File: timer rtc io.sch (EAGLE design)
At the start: 78 parts, among them T1 BC547, U1 74HC245, U10 74HC688, U11 74LS30N, U12 74LS00N, U13 74HC32, U14 74HC04, U15 74HC08, U16 74HC688, U17 74HC138, U18 74HC138, U19 74HC573, U2 74HC245, U20 74HC573, U21 74HC573, U22 74HC573, U23 74HC573, U24 NE555, U3 74HC245, U4 74HC688, U6 74HC74, U7 74HC590, U8 74HC688, U9 BQ4845, X1 32.768KHz, Y1 4.096MHz

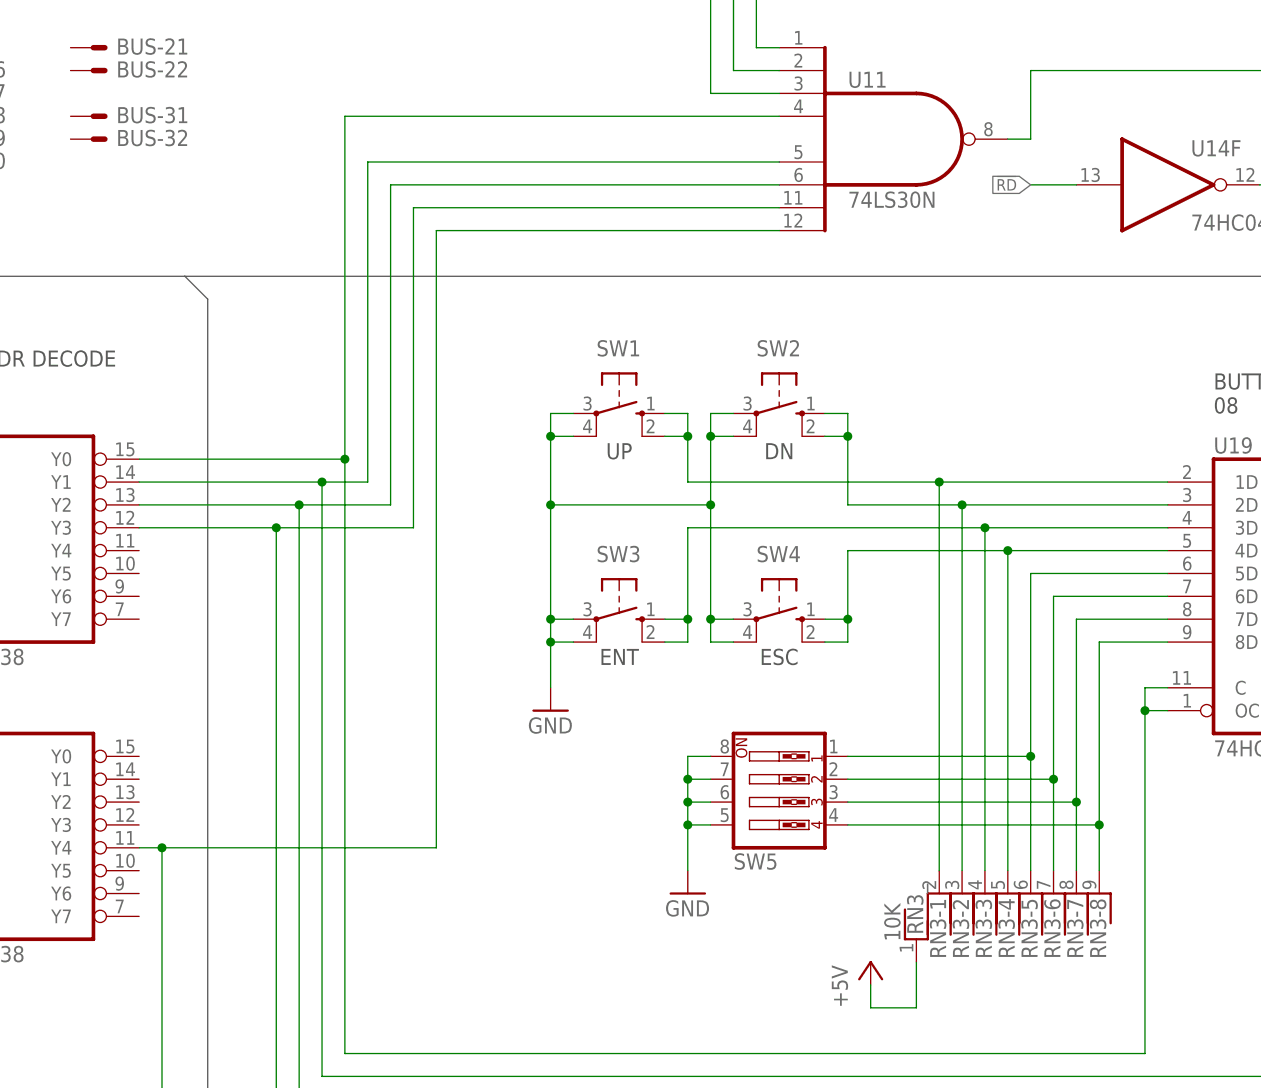
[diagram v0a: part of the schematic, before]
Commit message: Annotate SW5 DIP switch positions
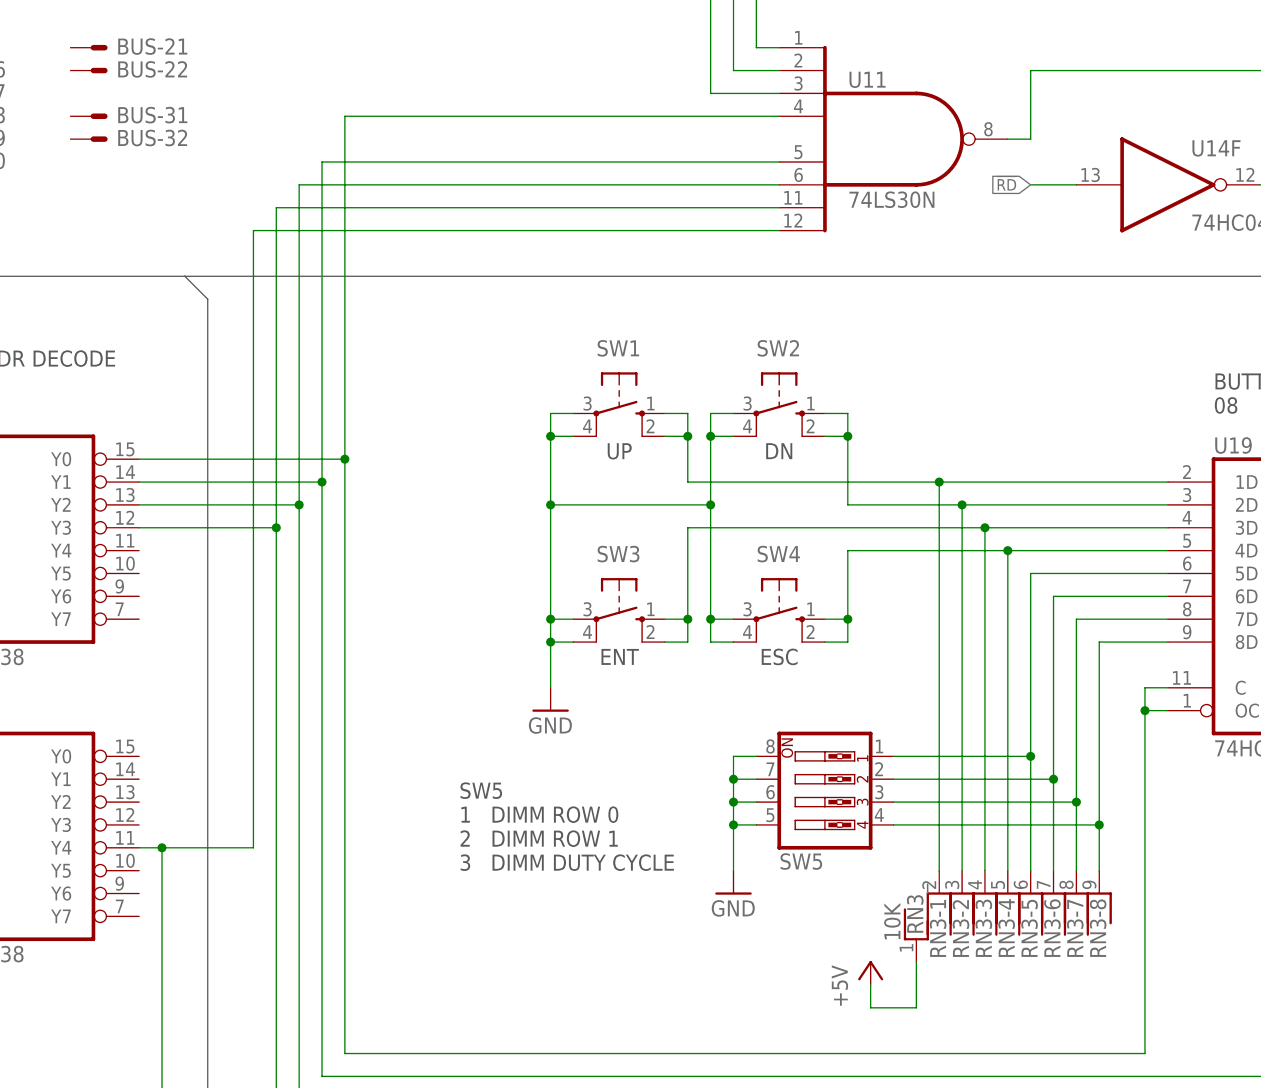
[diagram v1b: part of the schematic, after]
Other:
- note added: "SW5 1 DIMM ROW 0 2 DIMM ROW 1 3 DIMM DUTY CYCLE"
- note added: "TODO"
- moved on the sheet: SW5
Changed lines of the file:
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@@
 <?xml version="1.0" encoding="utf-8"?>
 <!DOCTYPE eagle SYSTEM "eagle.dtd">
-<eagle version="9.5.2">
+<eagle version="9.6.1">
 <drawing>
 <settings>
@@
 <text x="228.6" y="-139.7" size="1.778" layer="97">R4=560R R5=560R ~66% D/C ~8.6KHZ
 R4=1K5 R5=150R ~91% D/C ~8KHZ</text>
+<text x="208.28" y="-38.1" size="1.778" layer="97">SW5
+1   DIMM ROW 0
+2   DIMM ROW 1
+3   DIMM DUTY CYCLE</text>
+<text x="302.26" y="-137.16" size="3.81" layer="90">TODO</text>
 </plain>
 <instances>
@@
 <attribute name="VALUE" x="93.98" y="124.46" size="1.778" layer="96"/>
 </instance>
-<instance part="SW5" gate="A" x="243.84" y="-30.48" smashed="yes" rot="MR180">
-<attribute name="NAME" x="238.76" y="-36.195" size="1.778" layer="95" rot="MR180"/>
-<attribute name="VALUE" x="238.76" y="-20.32" size="1.778" layer="96" rot="MR180"/>
+<instance part="SW5" gate="A" x="248.92" y="-30.48" smashed="yes" rot="MR180">
+<attribute name="NAME" x="243.84" y="-36.195" size="1.778" layer="95" rot="MR180"/>
+<attribute name="VALUE" x="243.84" y="-20.32" size="1.778" layer="96" rot="MR180"/>
 </instance>
-<instance part="GND20" gate="1" x="233.68" y="-40.64" smashed="yes">
-<attribute name="VALUE" x="231.14" y="-43.18" size="1.778" layer="96"/>
+<instance part="GND20" gate="1" x="238.76" y="-40.64" smashed="yes">
+<attribute name="VALUE" x="236.22" y="-43.18" size="1.778" layer="96"/>
 </instance>
 <instance part="U16" gate="A" x="109.22" y="-17.78" smashed="yes">
@@
 <pinref part="SW5" gate="A" pin="8"/>
 <pinref part="GND20" gate="1" pin="GND"/>
-<wire x1="236.22" y1="-25.4" x2="233.68" y2="-25.4" width="0.1524" layer="91"/>
-<wire x1="233.68" y1="-25.4" x2="233.68" y2="-27.94" width="0.1524" layer="91"/>
+<wire x1="241.3" y1="-25.4" x2="238.76" y2="-25.4" width="0.1524" layer="91"/>
+<wire x1="238.76" y1="-25.4" x2="238.76" y2="-27.94" width="0.1524" layer="91"/>
 <pinref part="SW5" gate="A" pin="7"/>
-<wire x1="233.68" y1="-27.94" x2="233.68" y2="-30.48" width="0.1524" layer="91"/>
-<wire x1="233.68" y1="-30.48" x2="233.68" y2="-33.02" width="0.1524" layer="91"/>
-<wire x1="233.68" y1="-33.02" x2="233.68" y2="-38.1" width="0.1524" layer="91"/>
-<wire x1="236.22" y1="-27.94" x2="233.68" y2="-27.94" width="0.1524" layer="91"/>
-<junction x="233.68" y="-27.94"/>
+<wire x1="238.76" y1="-27.94" x2="238.76" y2="-30.48" width="0.1524" layer="91"/>
+<wire x1="238.76" y1="-30.48" x2="238.76" y2="-33.02" width="0.1524" layer="91"/>
+<wire x1="238.76" y1="-33.02" x2="238.76" y2="-38.1" width="0.1524" layer="91"/>
+<wire x1="241.3" y1="-27.94" x2="238.76" y2="-27.94" width="0.1524" layer="91"/>
+<junction x="238.76" y="-27.94"/>
 <pinref part="SW5" gate="A" pin="6"/>
-<wire x1="236.22" y1="-30.48" x2="233.68" y2="-30.48" width="0.1524" layer="91"/>
-<junction x="233.68" y="-30.48"/>
+<wire x1="241.3" y1="-30.48" x2="238.76" y2="-30.48" width="0.1524" layer="91"/>
+<junction x="238.76" y="-30.48"/>
 <pinref part="SW5" gate="A" pin="5"/>
-<wire x1="236.22" y1="-33.02" x2="233.68" y2="-33.02" width="0.1524" layer="91"/>
-<junction x="233.68" y="-33.02"/>
+<wire x1="241.3" y1="-33.02" x2="238.76" y2="-33.02" width="0.1524" layer="91"/>
+<junction x="238.76" y="-33.02"/>
 </segment>
 <segment>
@@
 <pinref part="SW5" gate="A" pin="1"/>
 <wire x1="271.78" y1="-25.4" x2="271.78" y2="-38.1" width="0.1524" layer="91"/>
-<wire x1="251.46" y1="-25.4" x2="271.78" y2="-25.4" width="0.1524" layer="91"/>
+<wire x1="256.54" y1="-25.4" x2="271.78" y2="-25.4" width="0.1524" layer="91"/>
 <junction x="271.78" y="-25.4"/>
 </segment>
@@
 <pinref part="SW5" gate="A" pin="2"/>
 <wire x1="274.32" y1="-27.94" x2="274.32" y2="-38.1" width="0.1524" layer="91"/>
-<wire x1="251.46" y1="-27.94" x2="274.32" y2="-27.94" width="0.1524" layer="91"/>
+<wire x1="256.54" y1="-27.94" x2="274.32" y2="-27.94" width="0.1524" layer="91"/>
 <junction x="274.32" y="-27.94"/>
 </segment>
@@
 <pinref part="SW5" gate="A" pin="3"/>
 <wire x1="276.86" y1="-30.48" x2="276.86" y2="-38.1" width="0.1524" layer="91"/>
-<wire x1="251.46" y1="-30.48" x2="276.86" y2="-30.48" width="0.1524" layer="91"/>
+<wire x1="256.54" y1="-30.48" x2="276.86" y2="-30.48" width="0.1524" layer="91"/>
 <junction x="276.86" y="-30.48"/>
 </segment>
@@
 <pinref part="SW5" gate="A" pin="4"/>
 <wire x1="279.4" y1="-33.02" x2="279.4" y2="-38.1" width="0.1524" layer="91"/>
-<wire x1="251.46" y1="-33.02" x2="279.4" y2="-33.02" width="0.1524" layer="91"/>
+<wire x1="256.54" y1="-33.02" x2="279.4" y2="-33.02" width="0.1524" layer="91"/>
 <junction x="279.4" y="-33.02"/>
 </segment>
@@
 <junction x="383.54" y="-20.32"/>
 <junction x="193.04" y="5.08"/>
-<wire x1="198.12" y1="5.08" x2="193.04" y2="5.08" width="0.1524" layer="91"/>
-<wire x1="198.12" y1="5.08" x2="198.12" y2="40.64" width="0.1524" layer="91"/>
-<wire x1="198.12" y1="40.64" x2="243.84" y2="40.64" width="0.1524" layer="91"/>
+<wire x1="193.04" y1="5.08" x2="193.04" y2="40.64" width="0.1524" layer="91"/>
+<wire x1="193.04" y1="40.64" x2="243.84" y2="40.64" width="0.1524" layer="91"/>
 <pinref part="U11" gate="A" pin="I4"/>
 </segment>
@@
 <wire x1="190.5" y1="-63.5" x2="482.6" y2="-63.5" width="0.1524" layer="91"/>
 <junction x="190.5" y="2.54"/>
-<wire x1="200.66" y1="2.54" x2="190.5" y2="2.54" width="0.1524" layer="91"/>
-<wire x1="200.66" y1="2.54" x2="200.66" y2="38.1" width="0.1524" layer="91"/>
+<wire x1="190.5" y1="2.54" x2="190.5" y2="38.1" width="0.1524" layer="91"/>
 <pinref part="U11" gate="A" pin="I5"/>
-<wire x1="200.66" y1="38.1" x2="243.84" y2="38.1" width="0.1524" layer="91"/>
+<wire x1="190.5" y1="38.1" x2="243.84" y2="38.1" width="0.1524" layer="91"/>
 <pinref part="U22" gate="A" pin="OC"/>
 <pinref part="U22" gate="A" pin="C"/>
@@
 <pinref part="U18" gate="A" pin="Y4"/>
 <wire x1="175.26" y1="-35.56" x2="172.72" y2="-35.56" width="0.1524" layer="91"/>
-<wire x1="175.26" y1="-35.56" x2="205.74" y2="-35.56" width="0.1524" layer="91"/>
+<wire x1="175.26" y1="-35.56" x2="185.42" y2="-35.56" width="0.1524" layer="91"/>
 <junction x="175.26" y="-35.56"/>
 <wire x1="144.78" y1="-104.14" x2="147.32" y2="-104.14" width="0.1524" layer="91"/>
 <pinref part="U12" gate="D" pin="I0"/>
-<wire x1="205.74" y1="-35.56" x2="205.74" y2="33.02" width="0.1524" layer="91"/>
+<wire x1="185.42" y1="-35.56" x2="185.42" y2="33.02" width="0.1524" layer="91"/>
 <pinref part="U11" gate="A" pin="I7"/>
-<wire x1="205.74" y1="33.02" x2="243.84" y2="33.02" width="0.1524" layer="91"/>
+<wire x1="185.42" y1="33.02" x2="243.84" y2="33.02" width="0.1524" layer="91"/>
 </segment>
 </net>
@@
 <wire x1="187.96" y1="-66.04" x2="383.54" y2="-66.04" width="0.1524" layer="91"/>
 <junction x="187.96" y="0"/>
-<wire x1="203.2" y1="0" x2="187.96" y2="0" width="0.1524" layer="91"/>
-<wire x1="203.2" y1="0" x2="203.2" y2="35.56" width="0.1524" layer="91"/>
+<wire x1="187.96" y1="0" x2="187.96" y2="35.56" width="0.1524" layer="91"/>
 <pinref part="U11" gate="A" pin="I6"/>
-<wire x1="203.2" y1="35.56" x2="243.84" y2="35.56" width="0.1524" layer="91"/>
+<wire x1="187.96" y1="35.56" x2="243.84" y2="35.56" width="0.1524" layer="91"/>
 <wire x1="383.54" y1="-111.76" x2="383.54" y2="-66.04" width="0.1524" layer="91"/>
 <junction x="383.54" y="-111.76"/>
